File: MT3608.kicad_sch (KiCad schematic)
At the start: 19 parts, among them J1 IN, J2 OUT, U1 MT3608

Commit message: Take 2
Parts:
- removed D1: SBR3U, Diode_SMD:D_PowerDI-123, symbol dmitriy:SBR3U60P1Q
- removed D2: 1N4148, Diode_THT:D_DO-35_SOD27_P7.62mm_Horizontal, symbol Diode:1N4148
- added D2: MBR0540, Diode_SMD:D_SOD-123, symbol Diode:MBR0540
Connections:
- net at C4.1, R1.1, R6.1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: now also D2.1 (K)
- net at L1.2, TP1.1, U1.1 (SW): now also D2.2 (A)
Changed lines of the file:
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@@
 (kicad_sch (version 20230121) (generator eeschema)
   (paper "A4")
-  (junction (at 168.91 76.835) (diameter 0) (color 0 0 0 0)
-  )
   (junction (at 191.77 107.315) (diameter 0) (color 0 0 0 0)
   )
@@
   (junction (at 191.77 86.36) (diameter 0) (color 0 0 0 0)
   )
-  (junction (at 141.605 76.835) (diameter 0) (color 0 0 0 0)
-  )
   (junction (at 100.33 86.36) (diameter 0) (color 0 0 0 0)
   )
@@
     (stroke (width 0) (type default))
   )
-  (wire (pts (xy 154.94 76.835) (xy 168.91 76.835))
-    (stroke (width 0) (type default))
-  )
-  (wire (pts (xy 141.605 76.835) (xy 141.605 76.2))
+  (wire (pts (xy 141.605 76.2) (xy 141.605 86.36))
     (stroke (width 0) (type default))
   )
@@
     (stroke (width 0) (type default))
   )
-  (wire (pts (xy 141.605 76.835) (xy 147.32 76.835))
-    (stroke (width 0) (type default))
-  )
   (wire (pts (xy 135.89 74.93) (xy 135.89 86.36))
     (stroke (width 0) (type default))
@@
   )
   (wire (pts (xy 112.395 74.93) (xy 112.395 86.36))
-    (stroke (width 0) (type default))
-  )
-  (wire (pts (xy 141.605 86.36) (xy 141.605 76.835))
     (stroke (width 0) (type default))
   )
@@
     )
   )
+  (symbol (lib_id "Diode:MBR0540") (at 151.13 86.36 180) (unit 1)
+    (in_bom yes) (on_board yes) (dnp no) (fields_autoplaced)
+    (property "Reference" "D2" (at 151.4475 80.645 0)
+      (effects (font (size 1.27 1.27)))
+    )
+    (property "Value" "MBR0540" (at 151.4475 83.185 0)
+      (effects (font (size 1.27 1.27)))
+    )
+    (property "Footprint" "Diode_SMD:D_SOD-123" (at 151.13 81.915 0)
+      (effects (font (size 1.27 1.27)) hide)
+    )
+    (property "Datasheet" "http://www.mccsemi.com/up_pdf/MBR0520~MBR0580(SOD123).pdf" (at 151.13 86.36 0)
+      (effects (font (size 1.27 1.27)) hide)
+    )
+    (pin "2")
+    (pin "1")
+    (instances
+      (project "MT3608"
+        (path "/cacd8407-0050-4646-8fae-b6e7c6c631e9"
+          (reference "D2") (unit 1)
+        )
+      )
+    )
+  )
   (symbol (lib_id "Connector:TestPoint") (at 130.175 104.775 0) (unit 1)
     (in_bom yes) (on_board yes) (dnp no) (fields_autoplaced)
@@
     )
   )
-  (symbol (lib_id "dmitriy:SBR3U60P1Q") (at 151.13 86.36 180) (unit 1)
-    (in_bom yes) (on_board yes) (dnp no) (fields_autoplaced)
-    (property "Reference" "D1" (at 151.4475 80.645 0)
-      (effects (font (size 1.27 1.27)))
-    )
-    (property "Value" "SBR3U" (at 151.4475 83.185 0)
-      (effects (font (size 1.27 1.27)))
-    )
-    (property "Footprint" "Diode_SMD:D_PowerDI-123" (at 151.13 91.44 0) (do_not_autoplace)
-      (effects (font (size 1.27 1.27)) hide)
-    )
-    (property "Datasheet" "https://www.diodes.com/assets/Datasheets/SBR3U60P1Q.pdf" (at 151.13 83.82 0)
-      (effects (font (size 1.27 1.27)) hide)
-    )
-    (pin "1")
-    (pin "2")
-    (instances
-      (project "MT3608"
-        (path "/cacd8407-0050-4646-8fae-b6e7c6c631e9"
-          (reference "D1") (unit 1)
-        )
-      )
-    )
-  )
   (symbol (lib_id "power:GND") (at 130.175 104.775 0) (unit 1)
     (in_bom yes) (on_board yes) (dnp no) (fields_autoplaced)
@@
         )
       )
-    )
-  )
-  (symbol (lib_id "Diode:1N4148") (at 151.13 76.835 180) (unit 1)
-    (in_bom yes) (on_board yes) (dnp no) (fields_autoplaced)
-    (property "Reference" "D2" (at 151.13 71.12 0)
-      (effects (font (size 1.27 1.27)))
-    )
-    (property "Value" "1N4148" (at 151.13 73.66 0)
-      (effects (font (size 1.27 1.27)))
-    )
-    (property "Footprint" "Diode_THT:D_DO-35_SOD27_P7.62mm_Horizontal" (at 151.13 76.835 0)
-      (effects (font (size 1.27 1.27)) hide)
-    )
-    (property "Datasheet" "https://assets.nexperia.com/documents/data-sheet/1N4148_1N4448.pdf" (at 151.13 76.835 0)
-      (effects (font (size 1.27 1.27)) hide)
-    )
-    (property "Sim.Device" "D" (at 151.13 76.835 0)
-      (effects (font (size 1.27 1.27)) hide)
-    )
-    (property "Sim.Pins" "1=K 2=A" (at 151.13 76.835 0)
-      (effects (font (size 1.27 1.27)) hide)
-    )
-    (pin "1")
-    (pin "2")
-    (instances
-      (project "MT3608"
-        (path "/cacd8407-0050-4646-8fae-b6e7c6c631e9"
-          (reference "D2") (unit 1)
-        )
-      )

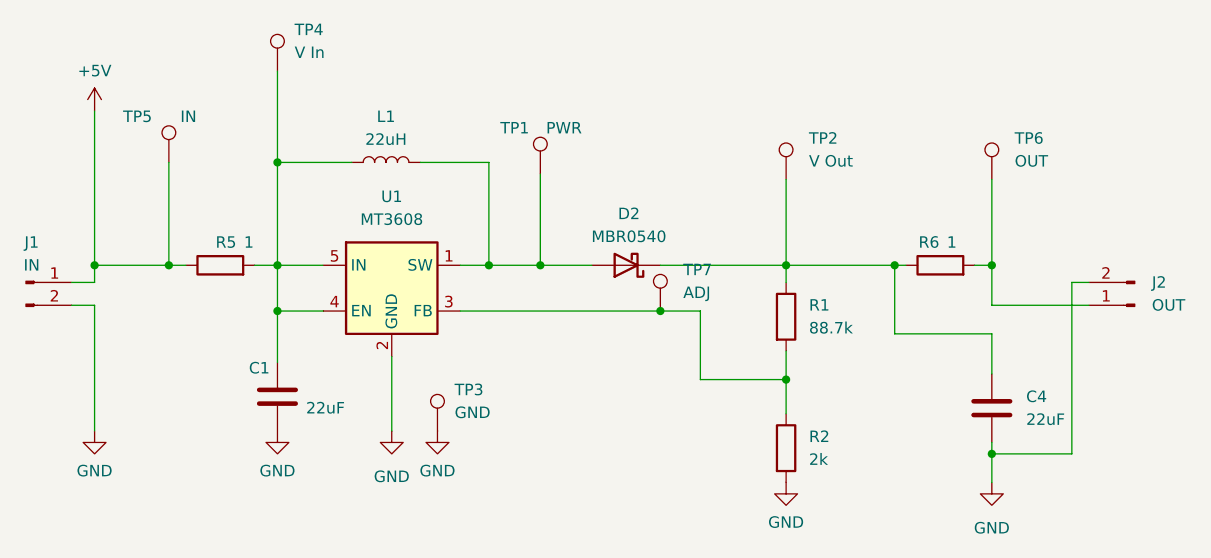
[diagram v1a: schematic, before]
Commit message: 27V works; corrected TP6
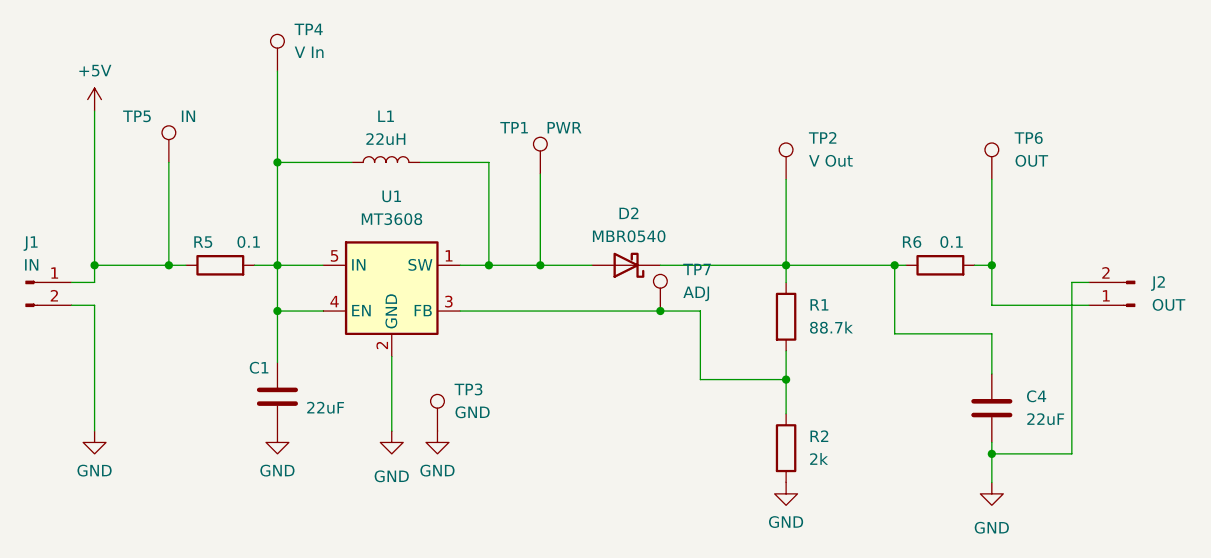
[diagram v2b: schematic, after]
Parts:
- C4: footprint Capacitor_SMD:C_0805_2012Metric_Pad1.18x1.45mm_HandSolder -> Capacitor_SMD:C_1206_3216Metric_Pad1.33x1.80mm_HandSolder
- R5, R6: value 1 -> 0.1
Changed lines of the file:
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@@
   (symbol (lib_id "Device:R") (at 106.045 86.36 90) (unit 1)
     (in_bom yes) (on_board yes) (dnp no)
-    (property "Reference" "R5" (at 106.68 83.82 90)
-      (effects (font (size 1.27 1.27)))
-    )
-    (property "Value" "1" (at 109.22 83.82 90)
+    (property "Reference" "R5" (at 104.14 83.82 90)
+      (effects (font (size 1.27 1.27)))
+    )
+    (property "Value" "0.1" (at 109.22 83.82 90)
       (effects (font (size 1.27 1.27)))
     )
@@
       (effects (font (size 1.27 1.27)) (justify left))
     )
-    (property "Footprint" "Capacitor_SMD:C_0805_2012Metric_Pad1.18x1.45mm_HandSolder" (at 192.7352 106.045 0)
+    (property "Footprint" "Capacitor_SMD:C_1206_3216Metric_Pad1.33x1.80mm_HandSolder" (at 192.7352 106.045 0)
       (effects (font (size 1.27 1.27)) hide)
     )
@@
   (symbol (lib_id "Device:R") (at 186.055 86.36 90) (unit 1)
     (in_bom yes) (on_board yes) (dnp no)
-    (property "Reference" "R6" (at 184.785 83.82 90)
-      (effects (font (size 1.27 1.27)))
-    )
-    (property "Value" "1" (at 187.325 83.82 90)
-      (effects (font (size 1.27 1.27)))
-    )
+    (property "Reference" "R6" (at 182.88 83.82 90)
+      (effects (font (size 1.27 1.27)))
+    )
+    (property "Value" "0.1" (at 187.325 83.82 90)
+      (effects (font (size 1.27 1.27)))
+    )
